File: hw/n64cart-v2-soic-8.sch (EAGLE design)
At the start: 40 parts, among them IC1 RP2040-QFN56, J1 N64_EDGE, Q1 BSS84, U1 W25Q128JVSIQ, U3 W25Q256JVEIQ_TR

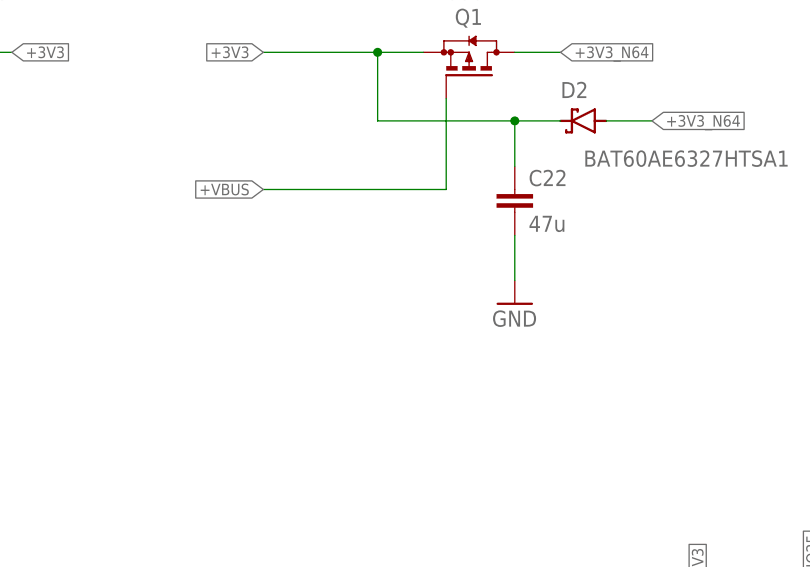
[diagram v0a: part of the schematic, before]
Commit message: missed pulldown resistor for V2
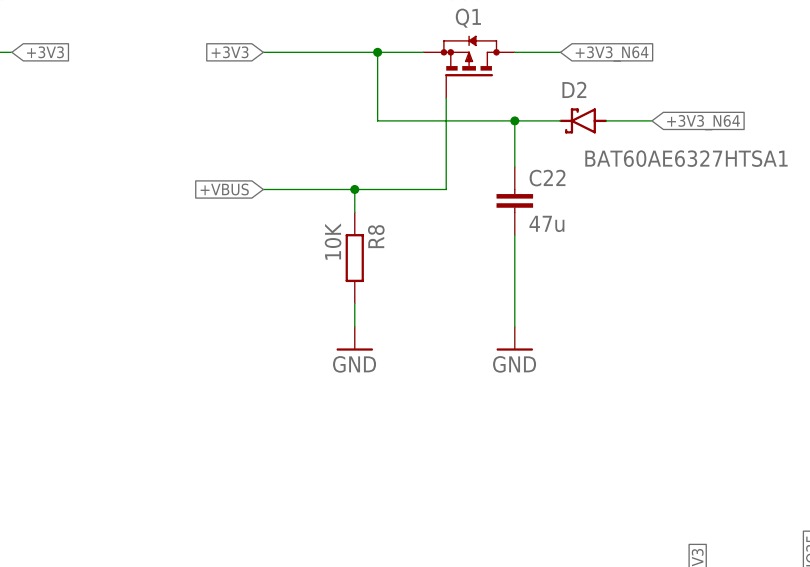
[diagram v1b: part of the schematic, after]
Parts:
- added R8: 10K, rcl:R-EU_R0402
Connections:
- net +VBUS: now also R8.1
- net GND: now also R8.2
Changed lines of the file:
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@@
 <part name="GND27" library="supply1" library_urn="urn:adsk.eagle:library:371" deviceset="GND" device=""/>
 <part name="C7" library="rcl" library_urn="urn:adsk.eagle:library:334" deviceset="C-EU" device="C0402" package3d_urn="urn:adsk.eagle:package:23626/2" value="100n"/>
+<part name="R8" library="rcl" library_urn="urn:adsk.eagle:library:334" deviceset="R-EU_" device="R0402" package3d_urn="urn:adsk.eagle:package:23547/3" value="10K"/>
+<part name="GND28" library="supply1" library_urn="urn:adsk.eagle:library:371" deviceset="GND" device=""/>
 </parts>
 <sheets>
@@
 <attribute name="VALUE" x="583.184" y="376.301" size="1.778" layer="96"/>
 </instance>
-<instance part="GND4" gate="1" x="581.66" y="368.3" smashed="yes">
-<attribute name="VALUE" x="579.12" y="365.76" size="1.778" layer="96"/>
+<instance part="GND4" gate="1" x="581.66" y="363.22" smashed="yes">
+<attribute name="VALUE" x="579.12" y="360.68" size="1.778" layer="96"/>
 </instance>
 <instance part="IC1" gate="IC$1" x="469.9" y="246.38" smashed="yes">
@@
 <attribute name="NAME" x="512.064" y="391.541" size="1.778" layer="95"/>
 <attribute name="VALUE" x="512.064" y="386.461" size="1.778" layer="96"/>
+</instance>
+<instance part="R8" gate="G$1" x="563.88" y="373.38" smashed="yes" rot="R270">
+<attribute name="NAME" x="565.3786" y="377.19" size="1.778" layer="95" rot="R270"/>
+<attribute name="VALUE" x="560.578" y="377.19" size="1.778" layer="96" rot="R270"/>
+</instance>
+<instance part="GND28" gate="1" x="563.88" y="363.22" smashed="yes">
+<attribute name="VALUE" x="561.34" y="360.68" size="1.778" layer="96"/>
 </instance>
 </instances>
@@
 <pinref part="C22" gate="G$1" pin="2"/>
 <pinref part="GND4" gate="1" pin="GND"/>
-<wire x1="581.66" y1="375.92" x2="581.66" y2="370.84" width="0.1524" layer="91"/>
+<wire x1="581.66" y1="375.92" x2="581.66" y2="365.76" width="0.1524" layer="91"/>
 </segment>
 <segment>
@@
 <pinref part="C4" gate="G$1" pin="2"/>
 <wire x1="469.9" y1="381" x2="469.9" y2="383.54" width="0.1524" layer="91"/>
+</segment>
+<segment>
+<pinref part="GND28" gate="1" pin="GND"/>
+<pinref part="R8" gate="G$1" pin="2"/>
+<wire x1="563.88" y1="365.76" x2="563.88" y2="368.3" width="0.1524" layer="91"/>
 </segment>
 </net>
@@
 <segment>
 <pinref part="Q1" gate="G$1" pin="G"/>
-<wire x1="553.72" y1="381" x2="574.04" y2="381" width="0.1524" layer="91"/>
+<wire x1="553.72" y1="381" x2="563.88" y2="381" width="0.1524" layer="91"/>
+<wire x1="563.88" y1="381" x2="574.04" y2="381" width="0.1524" layer="91"/>
 <wire x1="574.04" y1="381" x2="574.04" y2="391.16" width="0.1524" layer="91"/>
 <label x="553.72" y="381" size="1.27" layer="95" rot="R180" xref="yes"/>
-</segment>
-<segment>
+<pinref part="R8" gate="G$1" pin="1"/>
+<wire x1="563.88" y1="378.46" x2="563.88" y2="381" width="0.1524" layer="91"/>
+<junction x="563.88" y="381"/>
+</segment>
+<segment>
